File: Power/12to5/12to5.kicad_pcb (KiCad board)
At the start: 2 copper layers, 42.9 x 35.1 mm, 9 parts, among them CON1 BARREL_JACK, CON2 BARREL_JACK, CON3 BARREL_JACK, U1 LM1085, U2 USB1

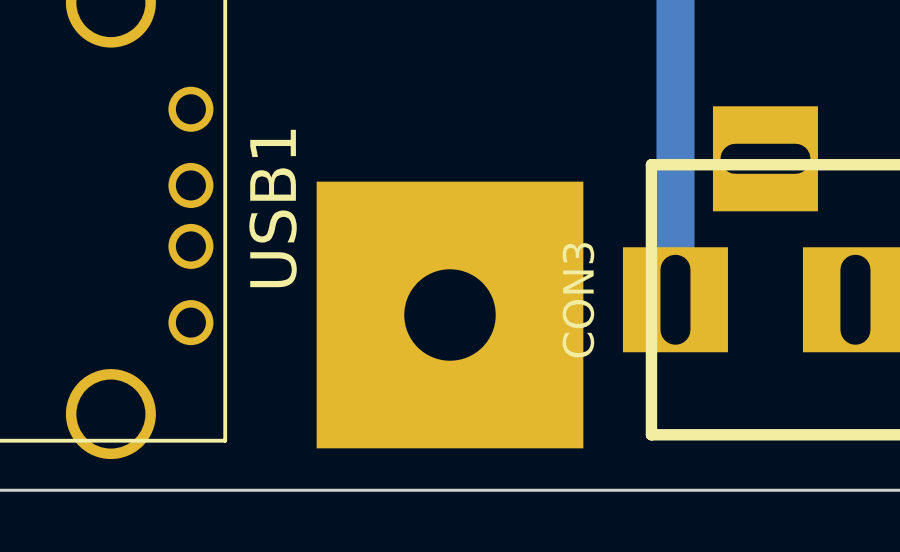
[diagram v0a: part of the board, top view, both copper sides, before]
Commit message: Updated LM1085 to be use SMD tab but throughole pins Fixed Text
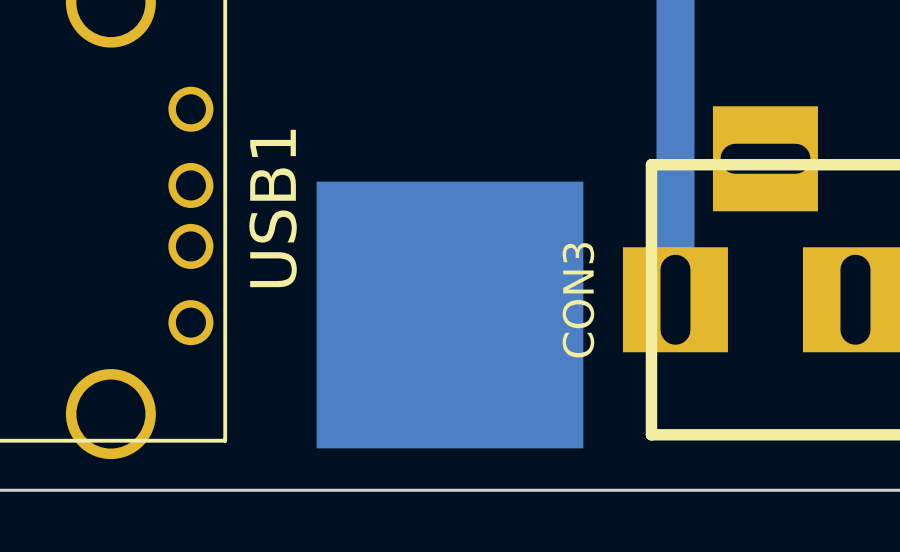
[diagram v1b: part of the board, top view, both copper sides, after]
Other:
- board text added: "+"
- board text added: "12to5"
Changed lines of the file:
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@@
     (area 169.346879 100.533999 212.923121 136.33418)
     (thickness 1.6)
-    (drawings 11)
+    (drawings 14)
     (tracks 20)
     (zones 0)
@@
   (page A3)
   (layers
-    (15 F.Cu signal hide)
-    (0 B.Cu signal hide)
+    (15 F.Cu signal)
+    (0 B.Cu signal)
     (16 B.Adhes user)
     (17 F.Adhes user)
@@
     (19 F.Paste user)
     (20 B.SilkS user)
-    (21 F.SilkS user hide)
+    (21 F.SilkS user)
     (22 B.Mask user)
     (23 F.Mask user)
@@
     (mod_text_size 1 1)
     (mod_text_width 0.15)
-    (pad_size 1.5 1.5)
-    (pad_drill 0.6)
+    (pad_size 8.89 8.89)
+    (pad_drill 0)
     (pad_to_mask_clearance 0)
     (aux_axis_origin 0 0)
-    (visible_elements 7FFFFFDF)
+    (visible_elements 7FFFFCFF)
     (pcbplotparams
       (layerselection 284196865)
@@
       (net 3 GND)
     )
-    (pad 4 thru_hole rect (at 16.51 0 270) (size 8.89 8.89) (drill 3.048)
-      (layers *.Cu *.SilkS *.Mask)
+    (pad 4 smd rect (at 16.51 0 270) (size 8.89 8.89)
+      (layers B.Cu F.Paste B.Mask)
       (net 2 +5V)
     )
@@
     (at 194.564 108.204 90)
     (attr smd)
-    (fp_text reference C1 (at 0 0 90) (layer B.SilkS)
+    (fp_text reference C1 (at 3.302 0 180) (layer B.SilkS)
       (effects (font (size 0.762 0.762) (thickness 0.127)) (justify mirror))
     )
@@
     (at 191.262 108.204 90)
     (attr smd)
-    (fp_text reference C2 (at 0 0 90) (layer B.SilkS)
+    (fp_text reference C2 (at 3.302 0 180) (layer B.SilkS)
       (effects (font (size 0.762 0.762) (thickness 0.127)) (justify mirror))
     )
@@
     (at 187.96 108.204 90)
     (attr smd)
-    (fp_text reference R1 (at 0 0 90) (layer B.SilkS)
+    (fp_text reference R1 (at 3.302 0 180) (layer B.SilkS)
       (effects (font (size 0.762 0.762) (thickness 0.127)) (justify mirror))
     )
@@
     )
   )
-  (gr_text 2014-02 (at 206.756 134.112) (layer B.Mask)
+  (gr_text + (at 195.834 111.76) (layer B.SilkS)
     (effects (font (size 1.5 1.5) (thickness 0.3)) (justify mirror))
   )
-  (gr_text "Sam K\nRev 1.0" (at 174.752 102.616) (layer B.Mask)
+  (gr_text + (at 189.992 111.76) (layer B.SilkS)
     (effects (font (size 1.5 1.5) (thickness 0.3)) (justify mirror))
   )
+  (gr_text 2014-02 (at 206.756 134.112) (layer B.SilkS)
+    (effects (font (size 1.5 1.5) (thickness 0.3)) (justify mirror))
+  )
+  (gr_text "Sam K\nRev 1.0" (at 208.28 102.362) (layer B.SilkS)
+    (effects (font (size 1.5 1.5) (thickness 0.3)) (justify mirror))
+  )
+  (gr_text 12to5 (at 174.244 102.87) (layer B.SilkS)
+    (effects (font (size 1.5 1.5) (thickness 0.3)) (justify mirror))
+  )
